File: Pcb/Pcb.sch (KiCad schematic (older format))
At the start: 132 parts, among them J1 TRRS, Q1 2N7002, SW1 SW_Push, SW10 SW_Push, SW11 SW_Push, SW12 SW_Push, SW13 SW_Push, SW14 SW_Push, SW15 SW_Push, SW16 SW_Push, SW17 SW_Push, SW18 SW_Push, SW19 SW_Push, SW2 SW2, SW20 SW_Push, SW21 SW_Push, SW22 SW_Push, SW23 SW_Push, SW24 SW_Push, SW25 SW_Push, SW26 SW_Push, SW27 SW_Push, SW28 SW_Push, SW29 SW_Push, SW3 SW_Push, SW4 SW_Push, SW5 SW_Push, SW6 SW_Push, SW7 SW_Push, SW8 SW_Push, SW9 SW_Push, U1 ProMicro

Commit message: Update footprint
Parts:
- D1, D10, D11, D12, D13, D14, D15, D16, D17, D18, D19, D2, D20, D21, D22, D23, D24, D25, D26, D27, D28, D3, D4, D5, D6, D7, D8, D9: footprint Used_Footprints:Diode_SMD_TH -> Used_Footprints:Diode_Hybrid_SOD-123
- D29, D30, D31, D32, D33, D34, D35, D36, D37, D38, D39, D40, D41, D42, D43, D44, D45, D46, D47, D48, D49, D50, D51, D52, D53, D54, D55, D56: footprint Used_Footprints:LED -> Used_Footprints:LED_THT_1.8mm
- H1, H2, H3, H4, H5, H6, H7: footprint Used_Footprints:MountHole -> Used_Footprints:Hole_Mount_M4
- H8, H9: footprint Used_Footprints:CoverHole -> Used_Footprints:Hole_Cover_M2
- J1: footprint 1symblos:MJ-4PP-9_Dual -> Used_Footprints:TRSS_DUAL_THT
- JP2, JP3, JP4, JP5: footprint 1kbd:jumper -> 1symblos:Jumper
- Q1: footprint Used_Footprints:SOT-23 -> Used_Footprints:Mosfet_SMD_Dual_SOT-23
- R1, R10, R11, R12, R13, R14, R15, R16, R17, R18, R19, R2, R20, R21, R22, R23, R24, R25, R26, R27, R28, R29, R3, R30, R31, R4, R5, R6, R7, R8, R9: footprint Used_Footprints:Resistor_SMD_TH -> Used_Footprints:Resistor_Hybrid_1205
- SW1, SW10, SW11, SW12, SW13, SW14, SW15, SW16, SW17, SW18, SW19, SW2, SW20, SW21, SW22, SW23, SW24, SW25, SW26, SW27, SW28, SW3, SW4, SW5, SW6, SW7, SW8, SW9: footprint 1symblos:cherry -> Used_Footprints:Switch_MxAlpsChoc_MillMax_1u
- SW29: footprint Used_Footprints:Reset_Switch -> Used_Footprints:Switch_Reset_THT
- U1: footprint Used_Footprints:ProMicro_TwoSide -> Used_Footprints:ProMicro_Dual

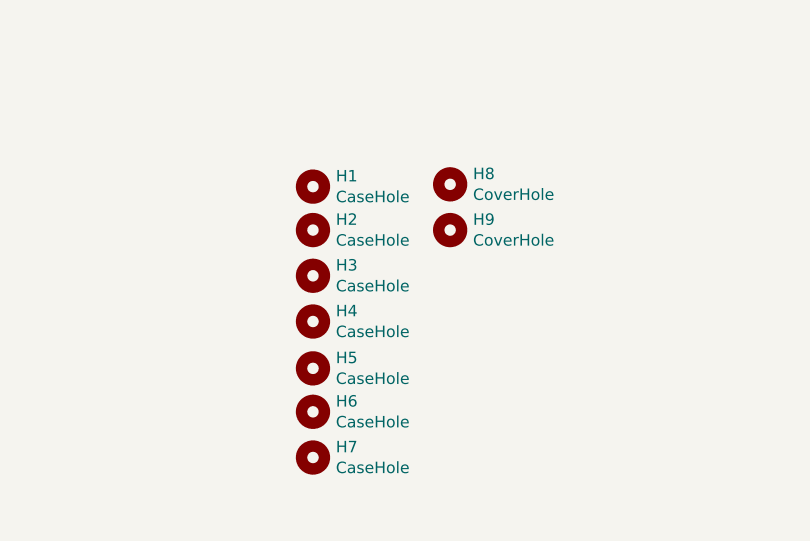
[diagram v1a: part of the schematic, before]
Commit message: Add one more mount hole
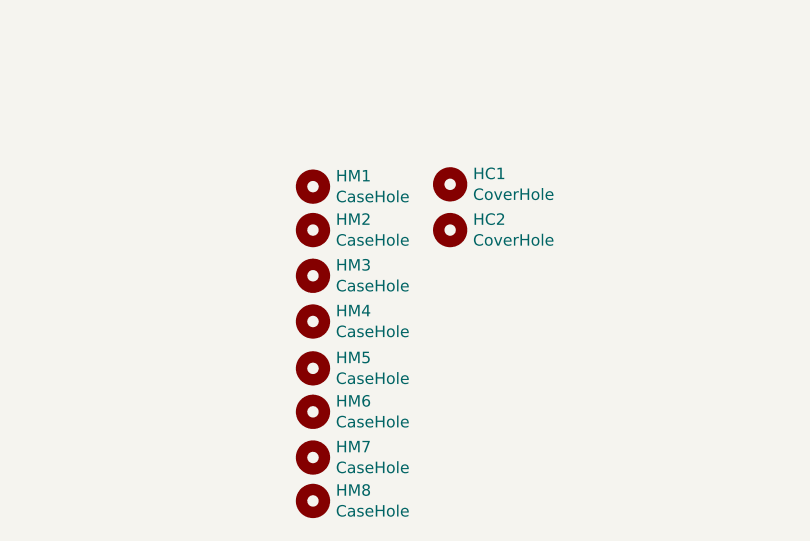
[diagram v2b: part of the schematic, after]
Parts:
- added HM8: CaseHole, Used_Footprints:Hole_Mount_M4, symbol Mechanical:MountingHole
- renumbered H8 to HC1, H9 to HC2, H1 to HM1, H2 to HM2, H3 to HM3, H4 to HM4, H5 to HM5, H6 to HM6, H7 to HM7
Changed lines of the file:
@@
 SCL
 $Comp
-L Mechanical:MountingHole H1
+L Mechanical:MountingHole HM1
 U 1 1 5DC03D38
 P 7515 4110
-F 0 "H1" H 7615 4156 50  0000 L CNN
+F 0 "HM1" H 7615 4156 50  0000 L CNN
 F 1 "CaseHole" H 7615 4065 50  0000 L CNN
 F 2 "Used_Footprints:Hole_Mount_M4" H 7515 4110 50  0001 C CNN
@@
 $EndComp
 $Comp
-L Mechanical:MountingHole H2
+L Mechanical:MountingHole HM2
 U 1 1 5DC0512E
 P 7515 4300
-F 0 "H2" H 7615 4346 50  0000 L CNN
+F 0 "HM2" H 7615 4346 50  0000 L CNN
 F 1 "CaseHole" H 7615 4255 50  0000 L CNN
 F 2 "Used_Footprints:Hole_Mount_M4" H 7515 4300 50  0001 C CNN
@@
 $EndComp
 $Comp
-L Mechanical:MountingHole H3
+L Mechanical:MountingHole HM3
 U 1 1 5DC0F92C
 P 7515 4500
-F 0 "H3" H 7615 4546 50  0000 L CNN
+F 0 "HM3" H 7615 4546 50  0000 L CNN
 F 1 "CaseHole" H 7615 4455 50  0000 L CNN
 F 2 "Used_Footprints:Hole_Mount_M4" H 7515 4500 50  0001 C CNN
@@
 $EndComp
 $Comp
-L Mechanical:MountingHole H4
+L Mechanical:MountingHole HM4
 U 1 1 5DC14B86
 P 7515 4700
-F 0 "H4" H 7615 4746 50  0000 L CNN
+F 0 "HM4" H 7615 4746 50  0000 L CNN
 F 1 "CaseHole" H 7615 4655 50  0000 L CNN
 F 2 "Used_Footprints:Hole_Mount_M4" H 7515 4700 50  0001 C CNN
@@
 $EndComp
 $Comp
-L Mechanical:MountingHole H5
+L Mechanical:MountingHole HM5
 U 1 1 5DC1BC70
 P 7515 4905
-F 0 "H5" H 7615 4951 50  0000 L CNN
+F 0 "HM5" H 7615 4951 50  0000 L CNN
 F 1 "CaseHole" H 7615 4860 50  0000 L CNN
 F 2 "Used_Footprints:Hole_Mount_M4" H 7515 4905 50  0001 C CNN
@@
 $EndComp
 $Comp
-L Mechanical:MountingHole H6
+L Mechanical:MountingHole HM6
 U 1 1 5DC1BC76
 P 7515 5095
-F 0 "H6" H 7615 5141 50  0000 L CNN
+F 0 "HM6" H 7615 5141 50  0000 L CNN
 F 1 "CaseHole" H 7615 5050 50  0000 L CNN
 F 2 "Used_Footprints:Hole_Mount_M4" H 7515 5095 50  0001 C CNN
@@
 $EndComp
 $Comp
-L Mechanical:MountingHole H7
+L Mechanical:MountingHole HM7
 U 1 1 5DC1BC7C
 P 7515 5295
-F 0 "H7" H 7615 5341 50  0000 L CNN
+F 0 "HM7" H 7615 5341 50  0000 L CNN
 F 1 "CaseHole" H 7615 5250 50  0000 L CNN
 F 2 "Used_Footprints:Hole_Mount_M4" H 7515 5295 50  0001 C CNN
@@
 $EndComp
 $Comp
-L Mechanical:MountingHole H8
+L Mechanical:MountingHole HC1
 U 1 1 5DC2660A
 P 8115 4100
-F 0 "H8" H 8215 4146 50  0000 L CNN
+F 0 "HC1" H 8215 4146 50  0000 L CNN
 F 1 "CoverHole" H 8215 4055 50  0000 L CNN
 F 2 "Used_Footprints:Hole_Cover_M2" H 8115 4100 50  0001 C CNN
@@
 $EndComp
 $Comp
-L Mechanical:MountingHole H9
+L Mechanical:MountingHole HC2
 U 1 1 5DC26610
 P 8115 4300
-F 0 "H9" H 8215 4346 50  0000 L CNN
+F 0 "HC2" H 8215 4346 50  0000 L CNN
 F 1 "CoverHole" H 8215 4255 50  0000 L CNN
 F 2 "Used_Footprints:Hole_Cover_M2" H 8115 4300 50  0001 C CNN
@@
 	1    0    0    -1
 $EndComp
+$Comp
+L Mechanical:MountingHole HM8
+U 1 1 5E45ABA8
+P 7515 5485
+F 0 "HM8" H 7615 5531 50  0000 L CNN
+F 1 "CaseHole" H 7615 5440 50  0000 L CNN
+F 2 "Used_Footprints:Hole_Mount_M4" H 7515 5485 50  0001 C CNN
+F 3 "~" H 7515 5485 50  0001 C CNN
+	1    7515 5485
+	1    0    0    -1
+$EndComp

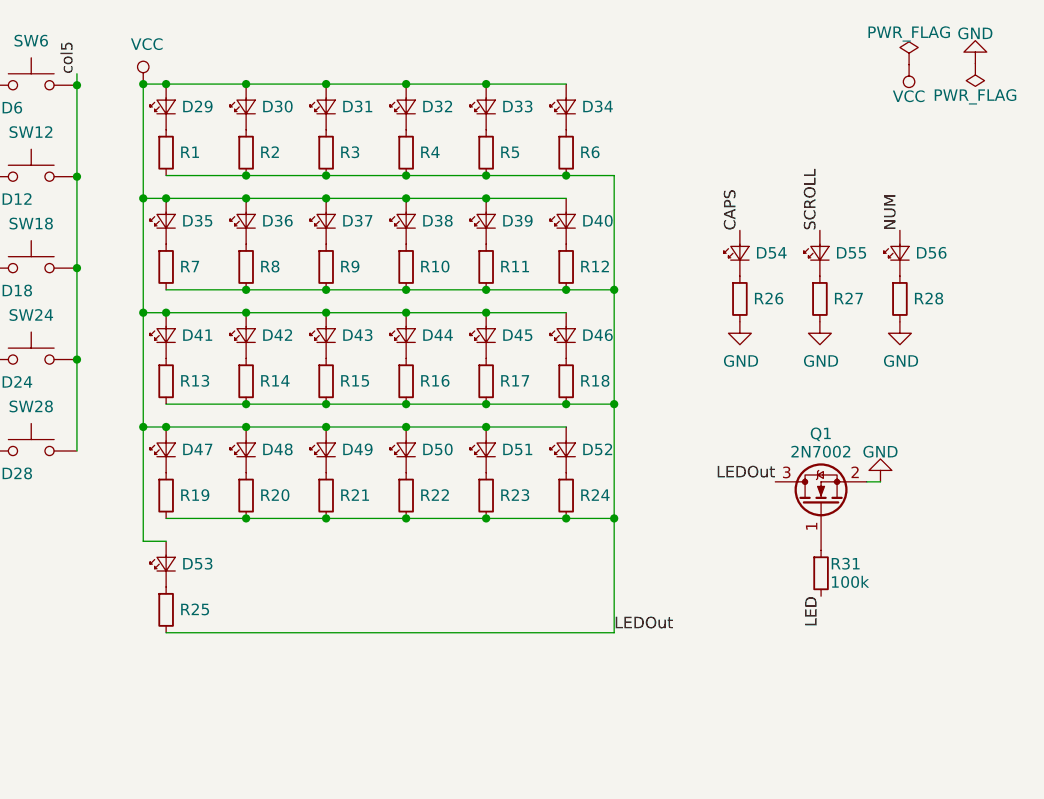
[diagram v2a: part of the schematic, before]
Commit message: Remove lock leds
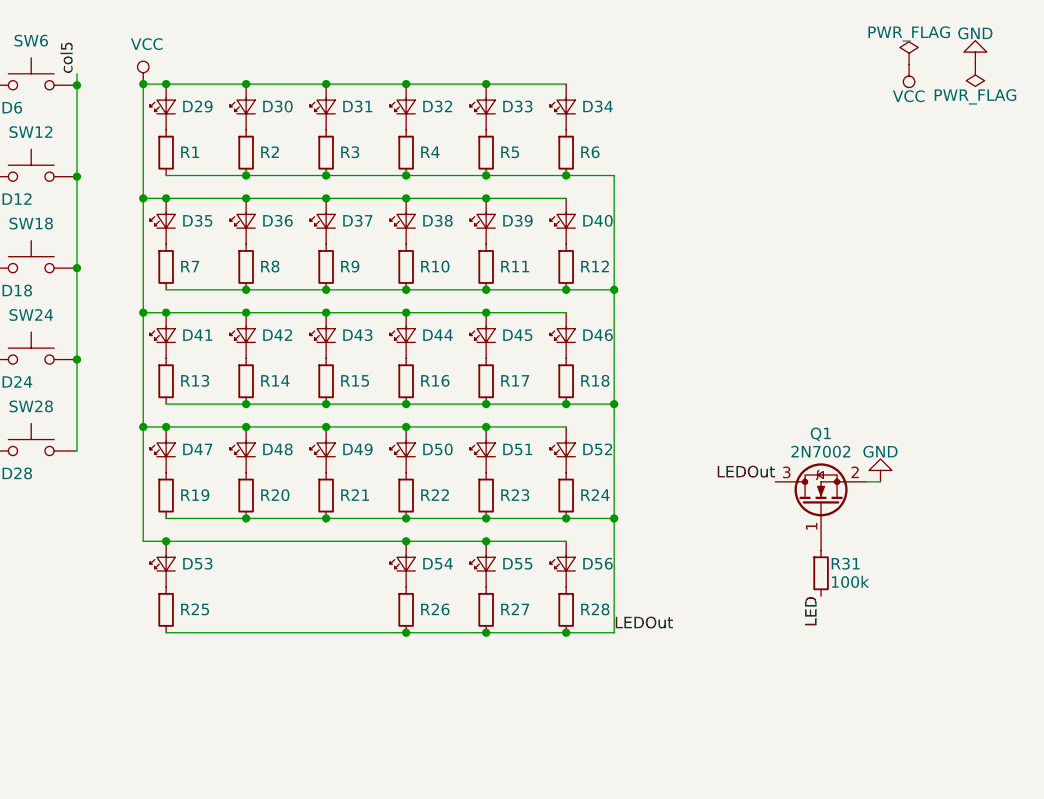
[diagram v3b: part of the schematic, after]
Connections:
- net CAPS: no longer D54.2 (A)
- net GND: no longer R26.2, R27.2, R28.2
- net LEDOut: now also R26.2, R27.2, R28.2
- net NUM: no longer D56.2 (A)
- net SCROLL: no longer D55.2 (A)
- net VCC: now also D54.2 (A), D55.2 (A), D56.2 (A)
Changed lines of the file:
@@
-$EndComp
-$Comp
-L Device:LED_Small D54
-U 1 1 5DB0079C
-P 9845 1625
-F 0 "D54" V 9845 1557 50  0000 R CNN
-F 1 "LED_Small" V 9800 1557 50  0001 R CNN
-F 2 "Used_Footprints:LED_THT_1.8mm" V 9845 1625 50  0001 C CNN
-F 3 "~" V 9845 1625 50  0001 C CNN
-	1    9845 1625
-	0    -1   -1   0
-$EndComp
-$Comp
-L Device:LED_Small D55
-U 1 1 5DB007A2
-P 10195 1625
-F 0 "D55" V 10195 1557 50  0000 R CNN
-F 1 "LED_Small" V 10150 1557 50  0001 R CNN
-F 2 "Used_Footprints:LED_THT_1.8mm" V 10195 1625 50  0001 C CNN
-F 3 "~" V 10195 1625 50  0001 C CNN
-	1    10195 1625
-	0    -1   -1   0
-$EndComp
-$Comp
-L Device:LED_Small D56
-U 1 1 5DB007A8
-P 10545 1625
-F 0 "D56" V 10545 1557 50  0000 R CNN
-F 1 "LED_Small" V 10500 1557 50  0001 R CNN
-F 2 "Used_Footprints:LED_THT_1.8mm" V 10545 1625 50  0001 C CNN
-F 3 "~" V 10545 1625 50  0001 C CNN
-	1    10545 1625
-	0    -1   -1   0
 $EndComp
 $Comp
@@
 F 3 "~" H 7335 3185 50  0001 C CNN
 	1    7335 3185
-	1    0    0    -1
-$EndComp
-$Comp
-L Device:R_Small R26
-U 1 1 5DB007C0
-P 9845 1825
-F 0 "R26" H 9904 1825 50  0000 L CNN
-F 1 "R_Small" H 9904 1780 50  0001 L CNN
-F 2 "Used_Footprints:Resistor_Hybrid_1205" H 9845 1825 50  0001 C CNN
-F 3 "~" H 9845 1825 50  0001 C CNN
-	1    9845 1825
-	1    0    0    -1
-$EndComp
-$Comp
-L Device:R_Small R27
-U 1 1 5DB007C6
-P 10195 1825
-F 0 "R27" H 10254 1825 50  0000 L CNN
-F 1 "R_Small" H 10254 1780 50  0001 L CNN
-F 2 "Used_Footprints:Resistor_Hybrid_1205" H 10195 1825 50  0001 C CNN
-F 3 "~" H 10195 1825 50  0001 C CNN
-	1    10195 1825
-	1    0    0    -1
-$EndComp
-$Comp
-L Device:R_Small R28
-U 1 1 5DB007CC
-P 10545 1825
-F 0 "R28" H 10604 1825 50  0000 L CNN
-F 1 "R_Small" H 10604 1780 50  0001 L CNN
-F 2 "Used_Footprints:Resistor_Hybrid_1205" H 10545 1825 50  0001 C CNN
-F 3 "~" H 10545 1825 50  0001 C CNN
-	1    10545 1825
 	1    0    0    -1
 $EndComp
@@
 	-1   0    0    1
 $EndComp
-Wire Wire Line
-	7335 3285 9295 3285
-$Comp
-L power:GND #PWR0103
-U 1 1 5DC0A2E9
-P 9845 1925
-F 0 "#PWR0103" H 9845 1675 50  0001 C CNN
-F 1 "GND" H 9850 1752 50  0000 C CNN
-F 2 "" H 9845 1925 50  0001 C CNN
-F 3 "" H 9845 1925 50  0001 C CNN
-	1    9845 1925
-	1    0    0    -1
-$EndComp
-$Comp
-L power:GND #PWR0104
-U 1 1 5DC0B2EF
-P 10195 1925
-F 0 "#PWR0104" H 10195 1675 50  0001 C CNN
-F 1 "GND" H 10200 1752 50  0000 C CNN
-F 2 "" H 10195 1925 50  0001 C CNN
-F 3 "" H 10195 1925 50  0001 C CNN
-	1    10195 1925
-	1    0    0    -1
-$EndComp
-$Comp
-L power:GND #PWR0105
-U 1 1 5DC0C10E
-P 10545 1925
-F 0 "#PWR0105" H 10545 1675 50  0001 C CNN
-F 1 "GND" H 10550 1752 50  0000 C CNN
-F 2 "" H 10545 1925 50  0001 C CNN
-F 3 "" H 10545 1925 50  0001 C CNN
-	1    10545 1925
-	1    0    0    -1
-$EndComp
-Text Label 9845 1525 1    50   ~ 0
-CAPS
-Text Label 10195 1525 1    50   ~ 0
-SCROLL
-Text Label 10545 1525 1    50   ~ 0
-NUM
 Text Label 2640 1745 0    50   ~ 0
 CAPS
@@
 	1    0    0    -1
 $EndComp
+$Comp
+L Device:LED_Small D54
+U 1 1 5E50A928
+P 8385 2985
+F 0 "D54" V 8385 2917 50  0000 R CNN
+F 1 "LED_Small" V 8340 2917 50  0001 R CNN
+F 2 "Used_Footprints:LED_THT_1.8mm" V 8385 2985 50  0001 C CNN
+F 3 "~" V 8385 2985 50  0001 C CNN
+	1    8385 2985
+	0    -1   -1   0
+$EndComp
+$Comp
+L Device:LED_Small D55
+U 1 1 5E50A92E
+P 8735 2985
+F 0 "D55" V 8735 2917 50  0000 R CNN
+F 1 "LED_Small" V 8690 2917 50  0001 R CNN
+F 2 "Used_Footprints:LED_THT_1.8mm" V 8735 2985 50  0001 C CNN
+F 3 "~" V 8735 2985 50  0001 C CNN
+	1    8735 2985
+	0    -1   -1   0
+$EndComp
+$Comp
+L Device:LED_Small D56
+U 1 1 5E50A934
+P 9085 2985
+F 0 "D56" V 9085 2917 50  0000 R CNN
+F 1 "LED_Small" V 9040 2917 50  0001 R CNN
+F 2 "Used_Footprints:LED_THT_1.8mm" V 9085 2985 50  0001 C CNN
+F 3 "~" V 9085 2985 50  0001 C CNN
+	1    9085 2985
+	0    -1   -1   0
+$EndComp
+$Comp
+L Device:R_Small R26
+U 1 1 5E50A93A
+P 8385 3185
+F 0 "R26" H 8444 3185 50  0000 L CNN
+F 1 "R_Small" H 8444 3140 50  0001 L CNN
+F 2 "Used_Footprints:Resistor_Hybrid_1205" H 8385 3185 50  0001 C CNN
+F 3 "~" H 8385 3185 50  0001 C CNN
+	1    8385 3185
+	1    0    0    -1
+$EndComp
+$Comp
+L Device:R_Small R27
+U 1 1 5E50A940
+P 8735 3185
+F 0 "R27" H 8794 3185 50  0000 L CNN
+F 1 "R_Small" H 8794 3140 50  0001 L CNN
+F 2 "Used_Footprints:Resistor_Hybrid_1205" H 8735 3185 50  0001 C CNN
+F 3 "~" H 8735 3185 50  0001 C CNN
+	1    8735 3185
+	1    0    0    -1
+$EndComp
+$Comp
+L Device:R_Small R28
+U 1 1 5E50A946
+P 9085 3185
+F 0 "R28" H 9144 3185 50  0000 L CNN
+F 1 "R_Small" H 9144 3140 50  0001 L CNN
+F 2 "Used_Footprints:Resistor_Hybrid_1205" H 9085 3185 50  0001 C CNN
+F 3 "~" H 9085 3185 50  0001 C CNN
+	1    9085 3185
+	1    0    0    -1
+$EndComp
+Wire Wire Line
+	9295 3285 9085 3285
+Wire Wire Line
+	9085 3285 8735 3285
+Connection ~ 9085 3285
+Wire Wire Line
+	8735 3285 8385 3285
+Connection ~ 8735 3285
+Wire Wire Line
+	8385 3285 7335 3285
+Connection ~ 8385 3285
+Wire Wire Line
+	9085 2885 8735 2885
+Connection ~ 7335 2885
+Connection ~ 8385 2885
+Wire Wire Line
+	8385 2885 7335 2885
+Connection ~ 8735 2885
+Wire Wire Line
+	8735 2885 8385 2885
 $EndSCHEMATC

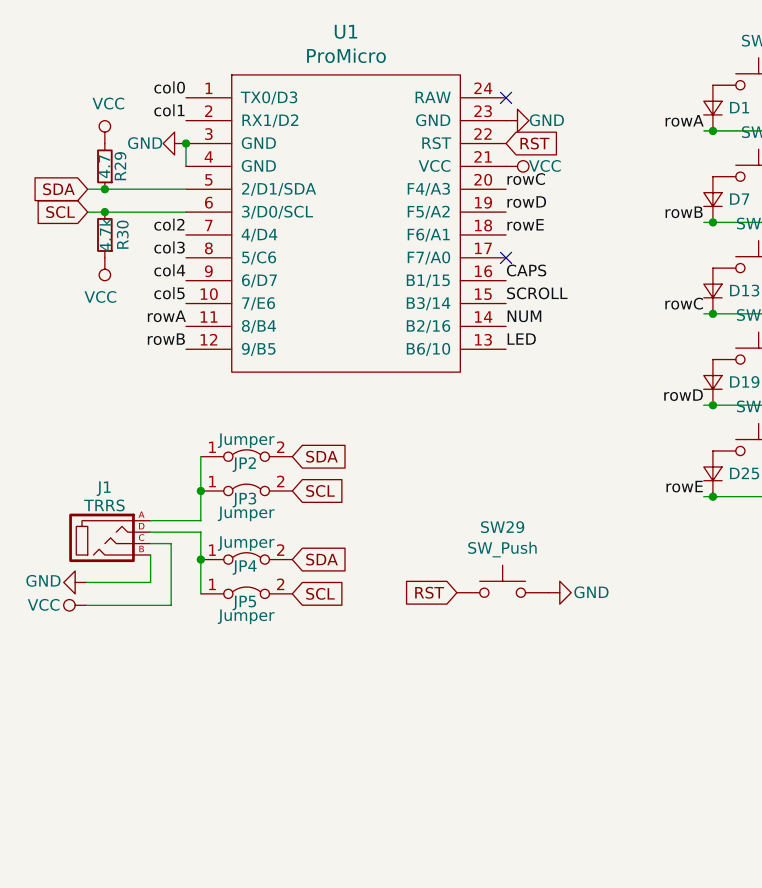
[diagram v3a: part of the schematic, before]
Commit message: Add JST pin for battery
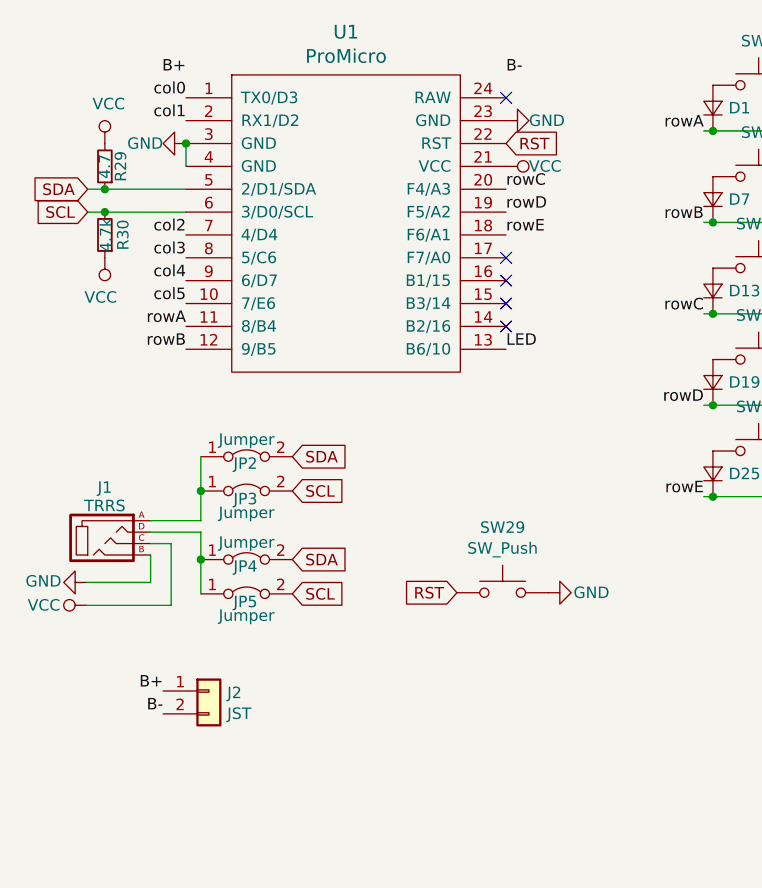
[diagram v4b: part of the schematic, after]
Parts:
- added J2: JST, symbol Connector_Generic:Conn_01x02
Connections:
- net CAPS: no longer names the net of U1.16 (B1/15)
- net NUM: no longer names the net of U1.14 (B2/16)
- net SCROLL: no longer names the net of U1.15 (B3/14)
- new net B+: J2.1 (Pin_1)
- new net B-: J2.2 (Pin_2)
- no-connect marks 2 -> 5
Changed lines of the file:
@@
 	-1   0    0    1
 $EndComp
-Text Label 2640 1745 0    50   ~ 0
-CAPS
-Text Label 2640 1845 0    50   ~ 0
-SCROLL
-Text Label 2640 1945 0    50   ~ 0
-NUM
 $Comp
 L power:GND #PWR0106
@@
 Wire Wire Line
 	8735 2885 8385 2885
+NoConn ~ 2640 1945
+NoConn ~ 2640 1845
+NoConn ~ 2640 1745
+Text Label 1240 845  2    50   ~ 0
+B+
+Text Label 2640 845  0    50   ~ 0
+B-
+$Comp
+L Connector_Generic:Conn_01x02 J2
+U 1 1 5E57C502
+P 1340 3540
+F 0 "J2" H 1420 3532 50  0000 L CNN
+F 1 "JST" H 1420 3441 50  0000 L CNN
+F 2 "" H 1340 3540 50  0001 C CNN
+F 3 "~" H 1340 3540 50  0001 C CNN
+	1    1340 3540
+	1    0    0    -1
+$EndComp
+Text Label 1140 3540 2    50   ~ 0
+B+
+Text Label 1140 3640 2    50   ~ 0
+B-
 $EndSCHEMATC
